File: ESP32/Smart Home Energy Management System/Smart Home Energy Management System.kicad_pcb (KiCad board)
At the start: 4 copper layers, 198.1 x 130.8 mm, 141 parts, among them J1 NEPA, J10 N, J11 PZEM_SIG, J14 USB_C Conn, J19 DISPLAY, J2 INVERTER, J20 LOAD 6, J21 LOAD 5, J22 LOAD 4, J23 LOAD 3, J24 LOAD 2, J25 LOAD 1, J3 CT, J6 PZEM_LOAD, K1 10A RELAY, K10 30A RELAY, K11 30A RELAY, K12 30A RELAY, K13 30A RELAY, K2 30A RELAY, K3 30A RELAY, K4 30A RELAY, K5 30A RELAY, K6 30A RELAY, K7 30A RELAY, K8 30A RELAY, K9 30A RELAY, Q1 UMH3N, Q2 UMH3N, Q3 ULN2803ADWR, Q4 ULN2803ADWR, SW1 RESET, SW2 FLASH, U1 LM2596S-3.3V, U2 LM2596S-12, U3 ESP32, U4 LM2596S-5V, U5 AMS1117-3.3, U6 PCA9555D, U7 CH340C, Y1 12MHz

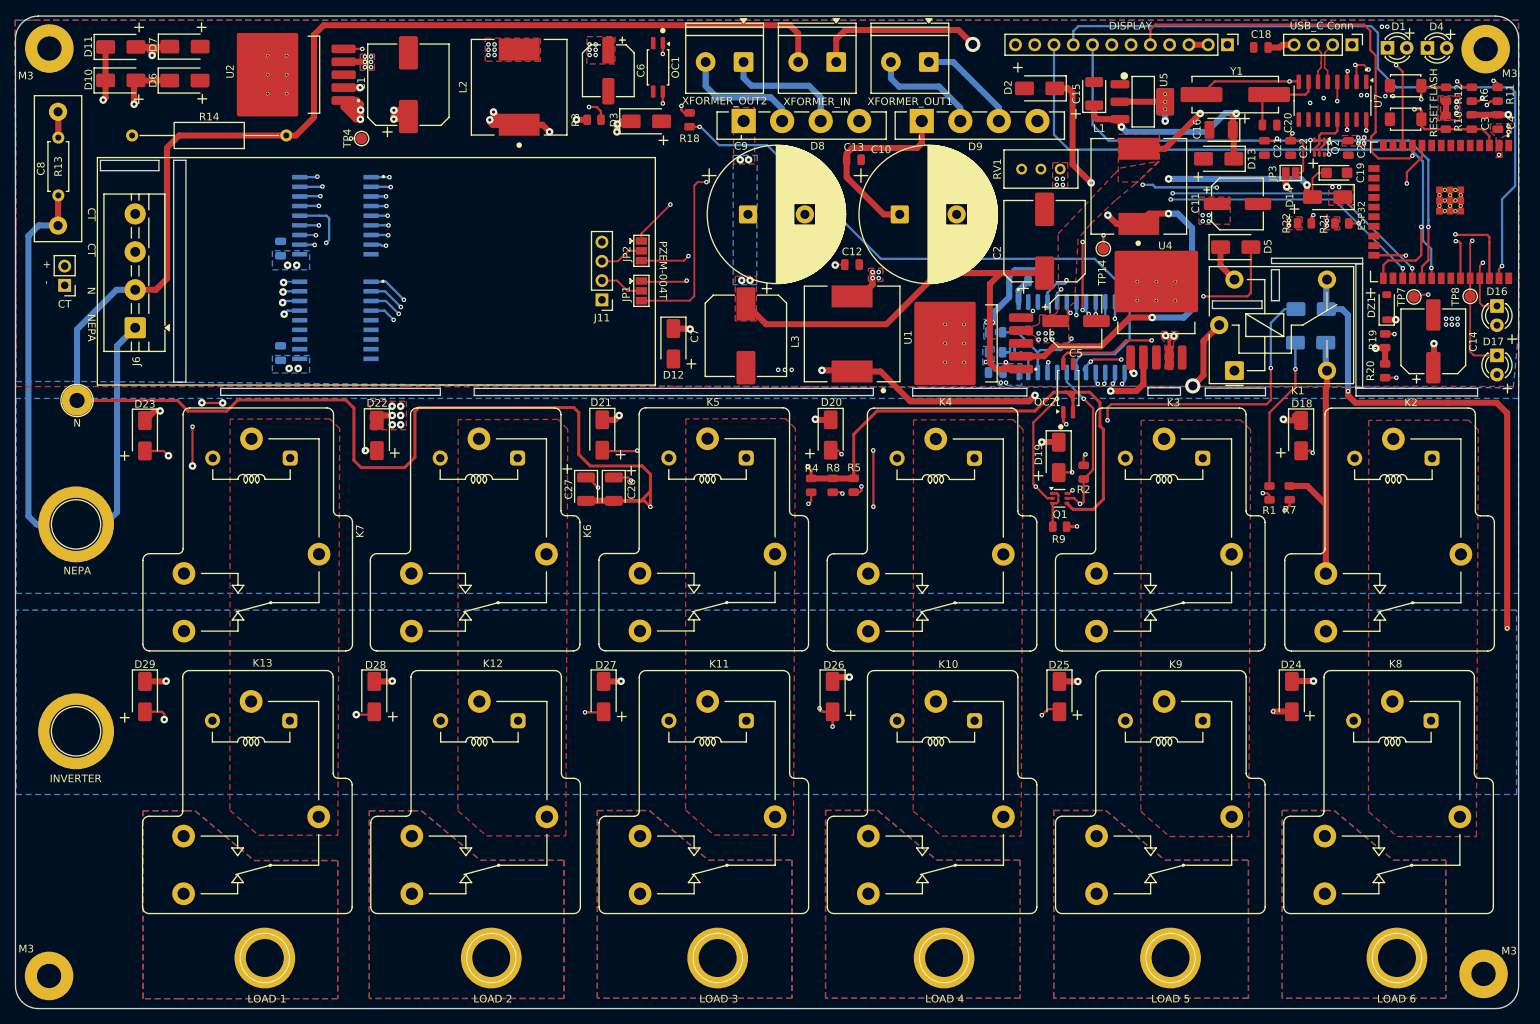
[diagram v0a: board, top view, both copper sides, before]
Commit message: Changing Blind/Buried Via into Through-hole type
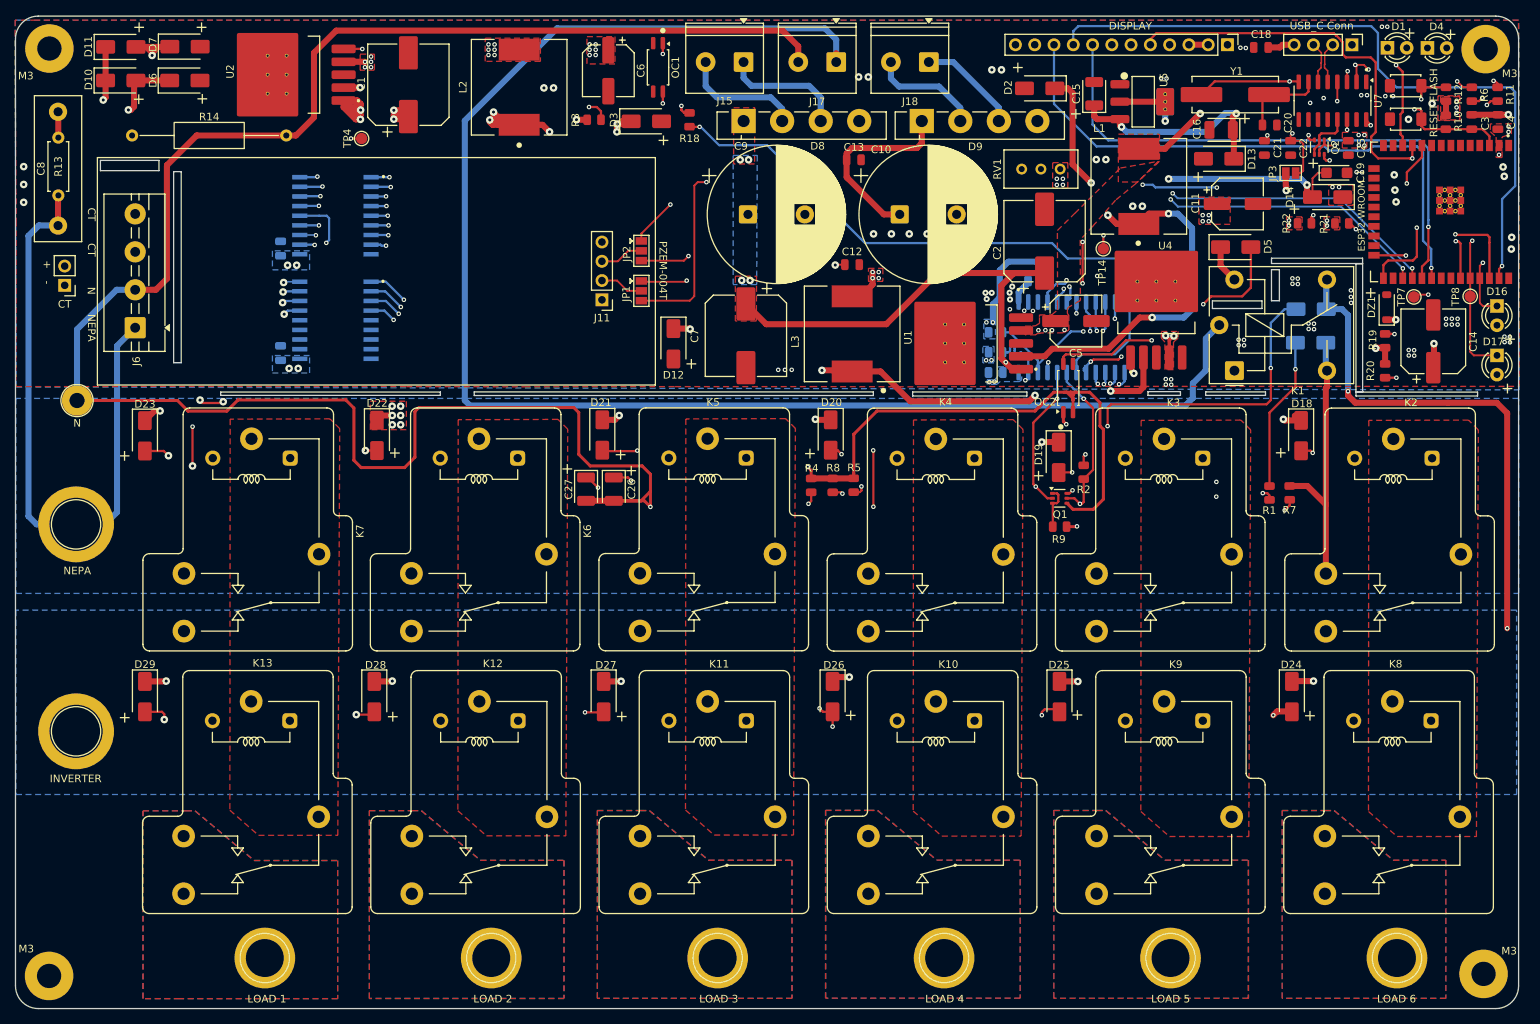
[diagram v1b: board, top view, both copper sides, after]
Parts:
- U3: value ESP32 -> ESP32-WROOM
- renumbered XFORMER_OUT2 to J15, XFORMER_IN to J17, XFORMER_OUT1 to J18
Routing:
- net /TRANS-IN: track 31.8 -> 203.3 mm, vias 2 -> 0
- net +12V: track 849.3 -> 886.2 mm, vias 39 -> 38
- net GND: track 6.22 -> 32.9 mm, vias 20 -> 90
- net /GPIO21/SDA: track 80.0 -> 90.4 mm
- net /N: track 353.2 -> 348.9 mm
- net +3.3V: track 82.4 -> 85.7 mm, vias 32 -> 30
- net /EN: track 28.1 -> 31.3 mm
- net Net-(Q3-IN3): track 108.3 -> 111.2 mm
- net Net-(JP3-A): track 20.0 -> 17.8 mm
- net Net-(U6-IO1_5): track 82.9 -> 84.9 mm
- net /GPIO22/SCL: track 91.7 -> 89.9 mm
- net /GPIO26: track 72.1 -> 70.5 mm
- net Net-(Q3-IN7): track 115.0 -> 113.6 mm
- net /GPIO18/SCK: track 77.8 -> 76.6 mm
- net Net-(Q4-IN1): track 108.9 -> 110.0 mm
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- added copper zone on In1.Cu, net VCC1
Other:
- outline, holes or cut-outs redrawn
